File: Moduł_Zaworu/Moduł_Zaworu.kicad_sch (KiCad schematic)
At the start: 10 parts, among them J2 RJ45, J3 RJ45, J9 Screw_Terminal_01x02, Q1 Q_NMOS, U11 ESP32-DEVKITC, U2 HHG1D-1

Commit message: Poprawki schematu modułu zaworu, usunięcie przekaźnika, przygotowanie schematu zasilania
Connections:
- net VSS: now reaches U2.1
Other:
- note added: "mosfet zamiast całego układu bo wystarczy jednostronna konwersja poziomów logicznych"
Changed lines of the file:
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@@
 	(generator_version "9.0")
 	(paper "A4")
+	(text "mosfet zamiast całego układu \nbo wystarczy jednostronna\n konwersja poziomów logicznych"
+		(exclude_from_sim no)
+		(at 129.54 44.45 0)
+		(effects
+			(font
+				(size 1.27 1.27)
+			)
+		)
+	)
 	(text "link RJ45"
 		(exclude_from_sim no)
@@
 	(wire
 		(pts
-			(xy 170.18 41.91) (xy 170.18 71.12)
+			(xy 170.18 40.64) (xy 170.18 71.12)
 		)
 		(stroke
@@
 					(unit 1)
 				)
+			)
+		)
+	)
+	(symbol
+		(lib_id "power:VSS")
+		(at 170.18 40.64 0)
+		(unit 1)
+		(exclude_from_sim no)
+		(in_bom yes)
+		(on_board yes)
+		(dnp no)
+		(fields_autoplaced yes)
+		(property "Reference" "#PWR018"
+			(at 170.18 44.45 0)
+			(effects
+				(font
+					(size 1.27 1.27)
+				)
+				(hide yes)
+			)
+		)
+		(property "Value" "VSS"
+			(at 170.18 35.56 0)
+			(effects
+				(font
+					(size 1.27 1.27)
+				)
+			)
+		)
+		(property "Footprint" ""
+			(at 170.18 40.64 0)
+			(effects
+				(font
+					(size 1.27 1.27)
+				)
+				(hide yes)
+			)
+		)
+		(property "Datasheet" ""
+			(at 170.18 40.64 0)
+			(effects
+				(font
+					(size 1.27 1.27)
+				)
+				(hide yes)
+			)
+		)
+		(property "Description" "Power symbol creates a global label with name \"VSS\""
+			(at 170.18 40.64 0)
+			(effects
+				(font
+					(size 1.27 1.27)
+				)
+				(hide yes)
+			)
+		)
+		(pin "1"
+		)
+		(instances
+			(project "Moduł_Zaworu"
+				(path "/8513fd68-b07b-4062-94bb-7b0327ec704f"
+					(reference "#PWR018")
+					(unit 1)
+				)

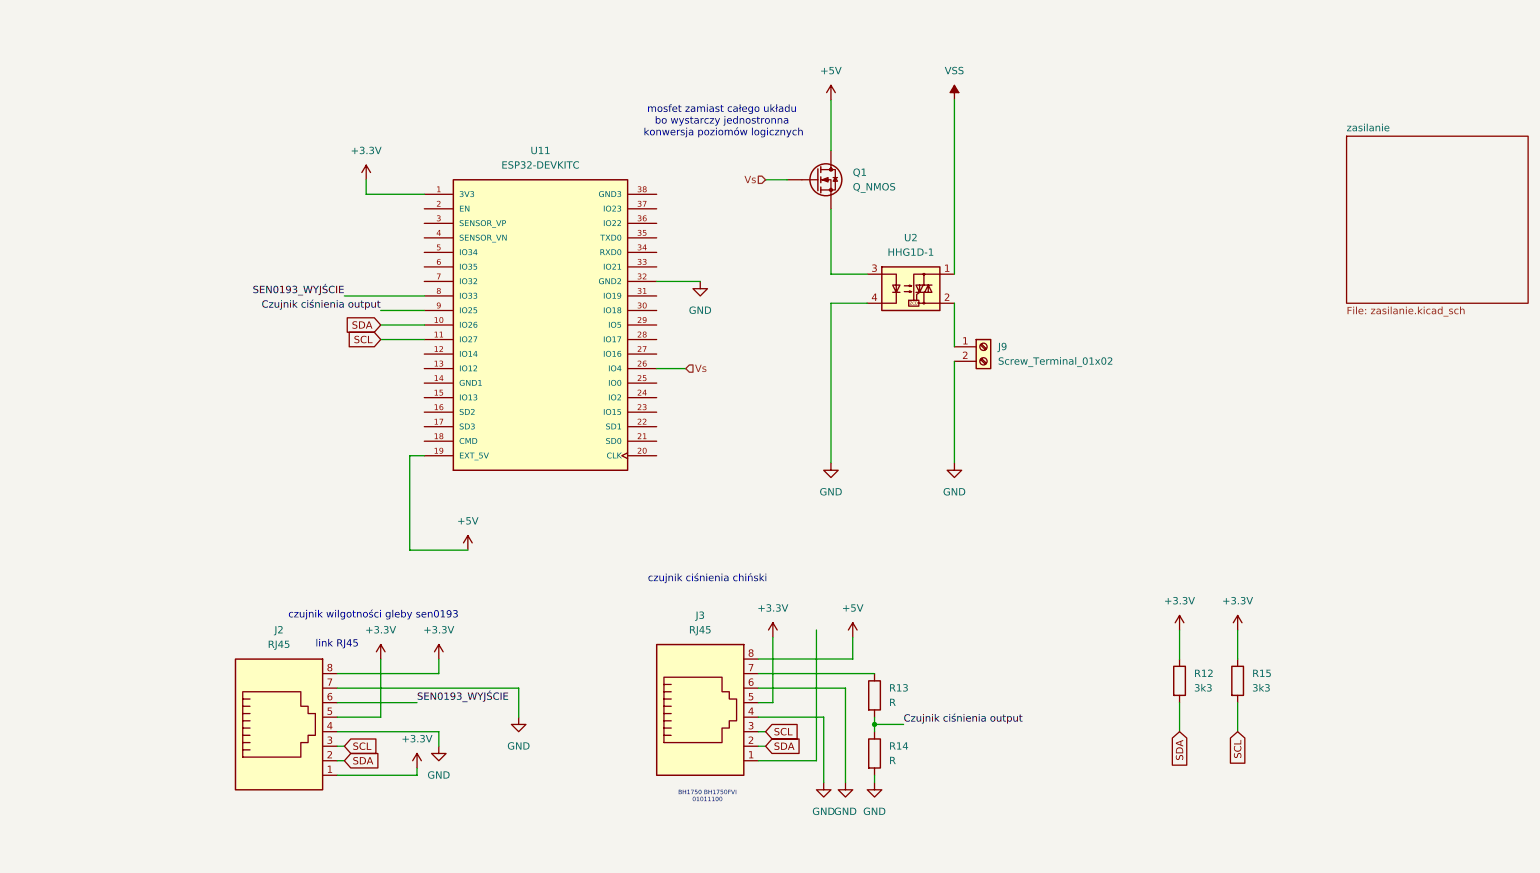
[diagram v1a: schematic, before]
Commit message: Poprawki schematu modułu zaworu, usunięcie przekaźnika, przygotowanie schematu zasilania
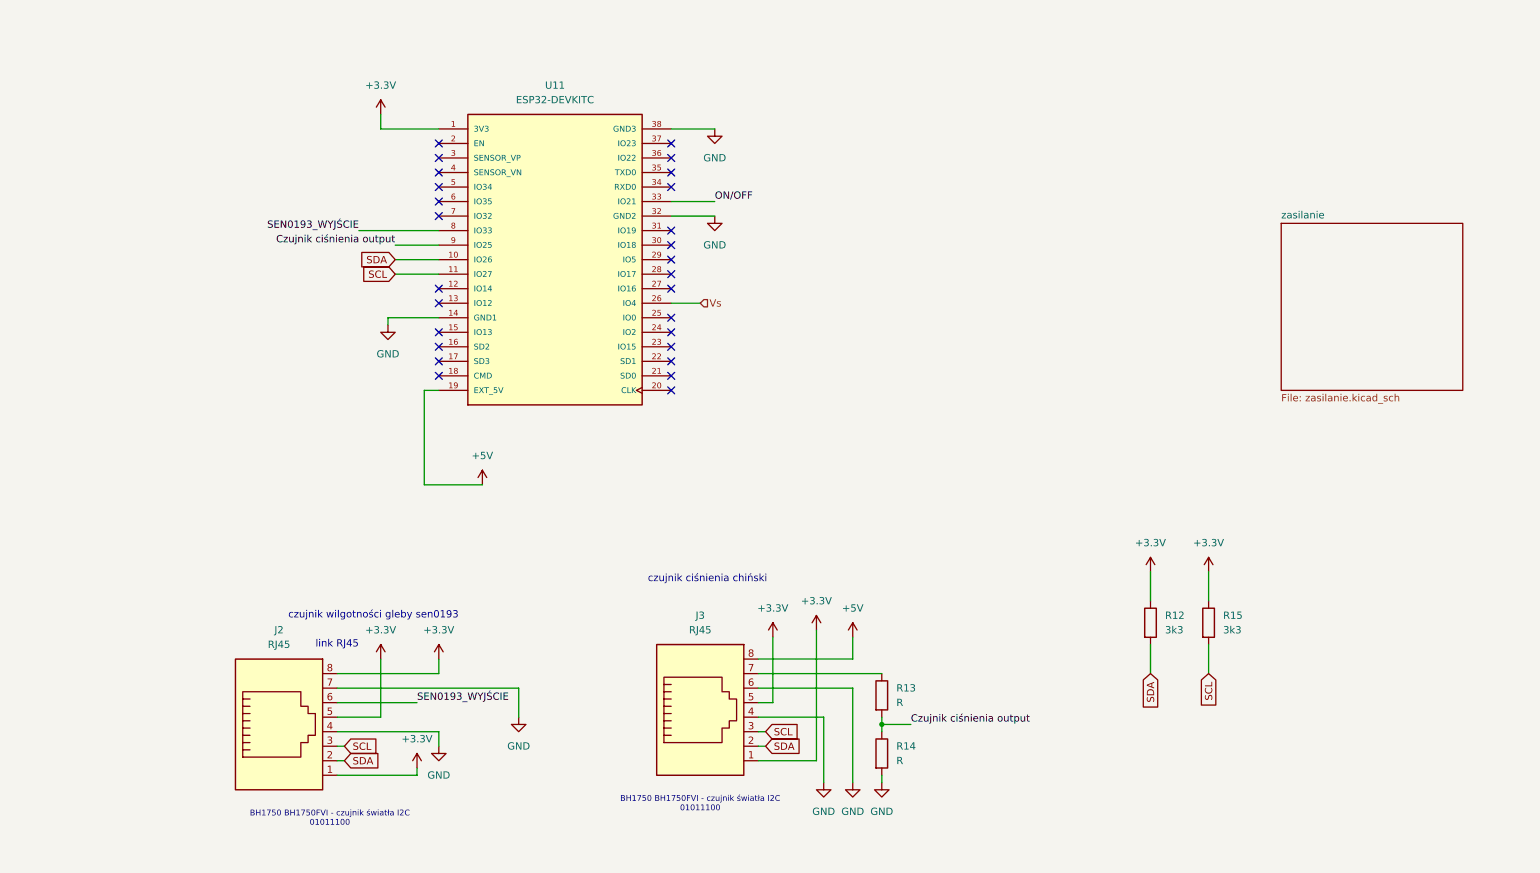
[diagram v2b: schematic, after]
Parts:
- removed J9: Screw_Terminal_01x02, TerminalBlock:TerminalBlock_MaiXu_MX126-5.0-02P_1x02_P5.00mm, symbol Connector:Screw_Terminal_01x02
- removed Q1: Q_NMOS, symbol Device:Q_NMOS
- removed U2: HHG1D-1, Relay_THT:RELAY_G3MB-202P, symbol Relay_SolidState:HHG1D-1
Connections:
- net +3.3V: now also J3.1
- net GND: now also U11.14 (GND1), U11.38 (GND3)
- net ON/OFF: now reaches U11.33 (IO21)
- no-connect marks 0 -> 27
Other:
- note added: "BH1750 BH1750FVI - czujnik światła I2C 01011100"
- note removed: "BH1750 BH1750FVI 01011100"
- note removed: "mosfet zamiast całego układu bo wystarczy jednostronna konwersja poziomów logicznych"
- moved on the sheet: R12, R13, R14, R15, U11

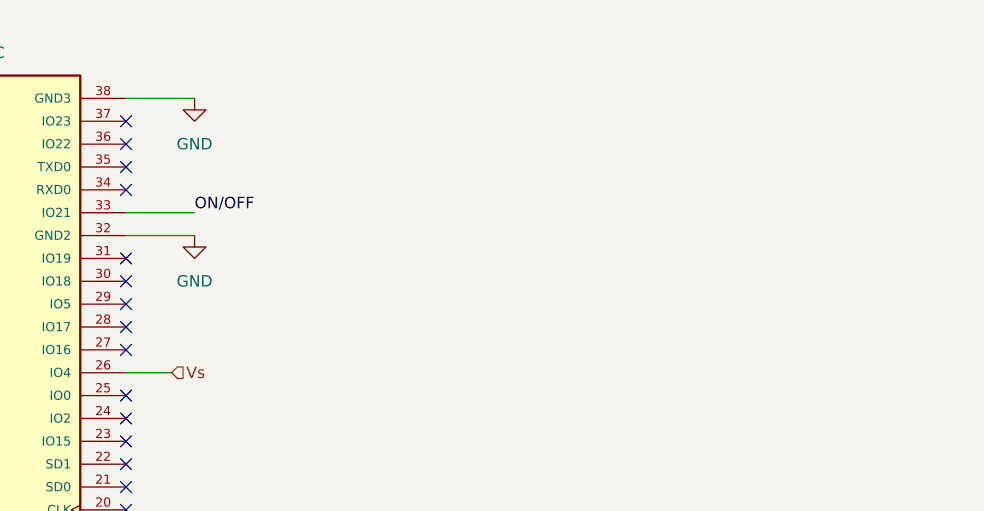
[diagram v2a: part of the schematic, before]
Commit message: Usunięcie zewnętrzego zasilania 12 i stabilizatora napięcia, korekcja zasilania wzmacniacz operacyjny moduł zasilania
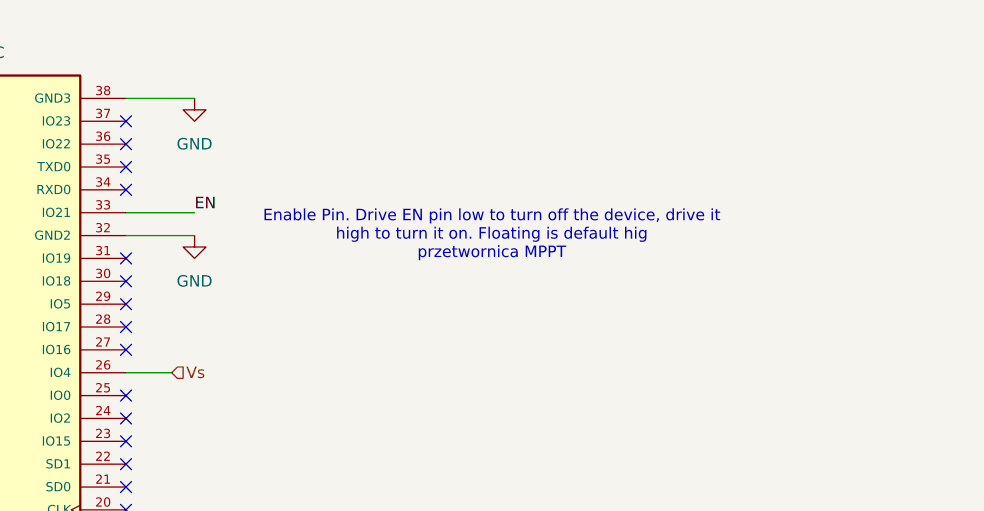
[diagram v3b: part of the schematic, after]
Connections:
- net ON/OFF renamed EN
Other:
- note added: "Enable Pin. Drive EN pin low to turn off the device, drive it high to turn it on. Floating is default hig przetwornica MPPT"
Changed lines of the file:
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@@
+		)
+	)
+	(text "Enable Pin. Drive EN pin low to turn off the device, drive it\nhigh to turn it on. Floating is default hig\nprzetwornica MPPT\n"
+		(exclude_from_sim no)
+		(at 161.29 60.96 0)
+		(effects
+			(font
+				(size 1.27 1.27)
+			)
 		)
 	)
@@
 		)
 	)
-	(label "ON{slash}OFF"
+	(label "EN"
 		(at 128.27 58.42 0)
 		(effects

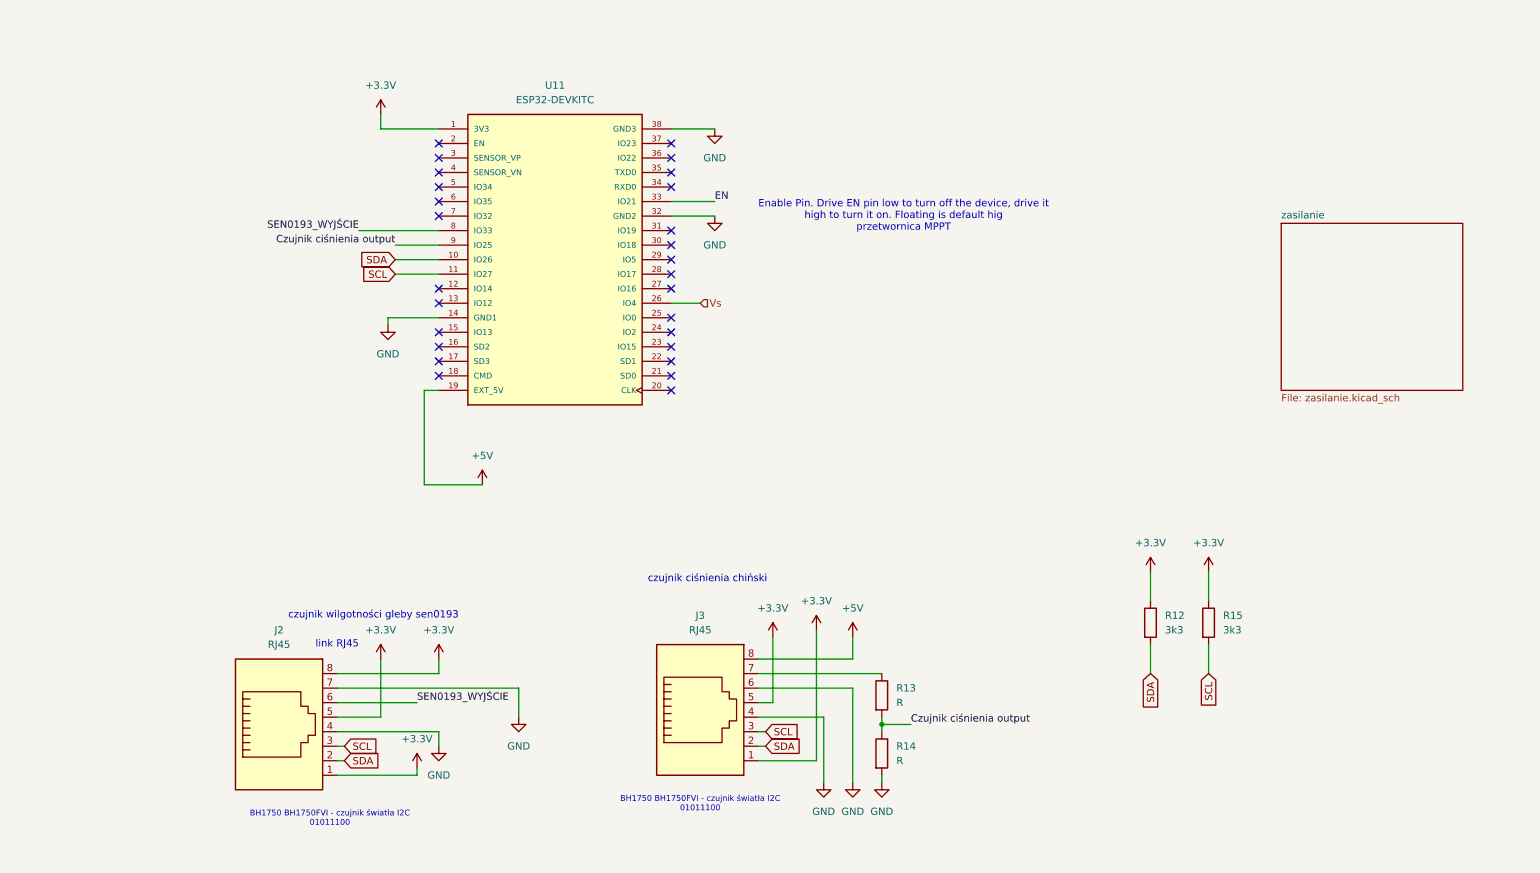
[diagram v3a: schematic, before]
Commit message: Poprawki moduł zasilania, stowrzenie płytki, zostało trochę błędów, zapomniałem dać mouting holes
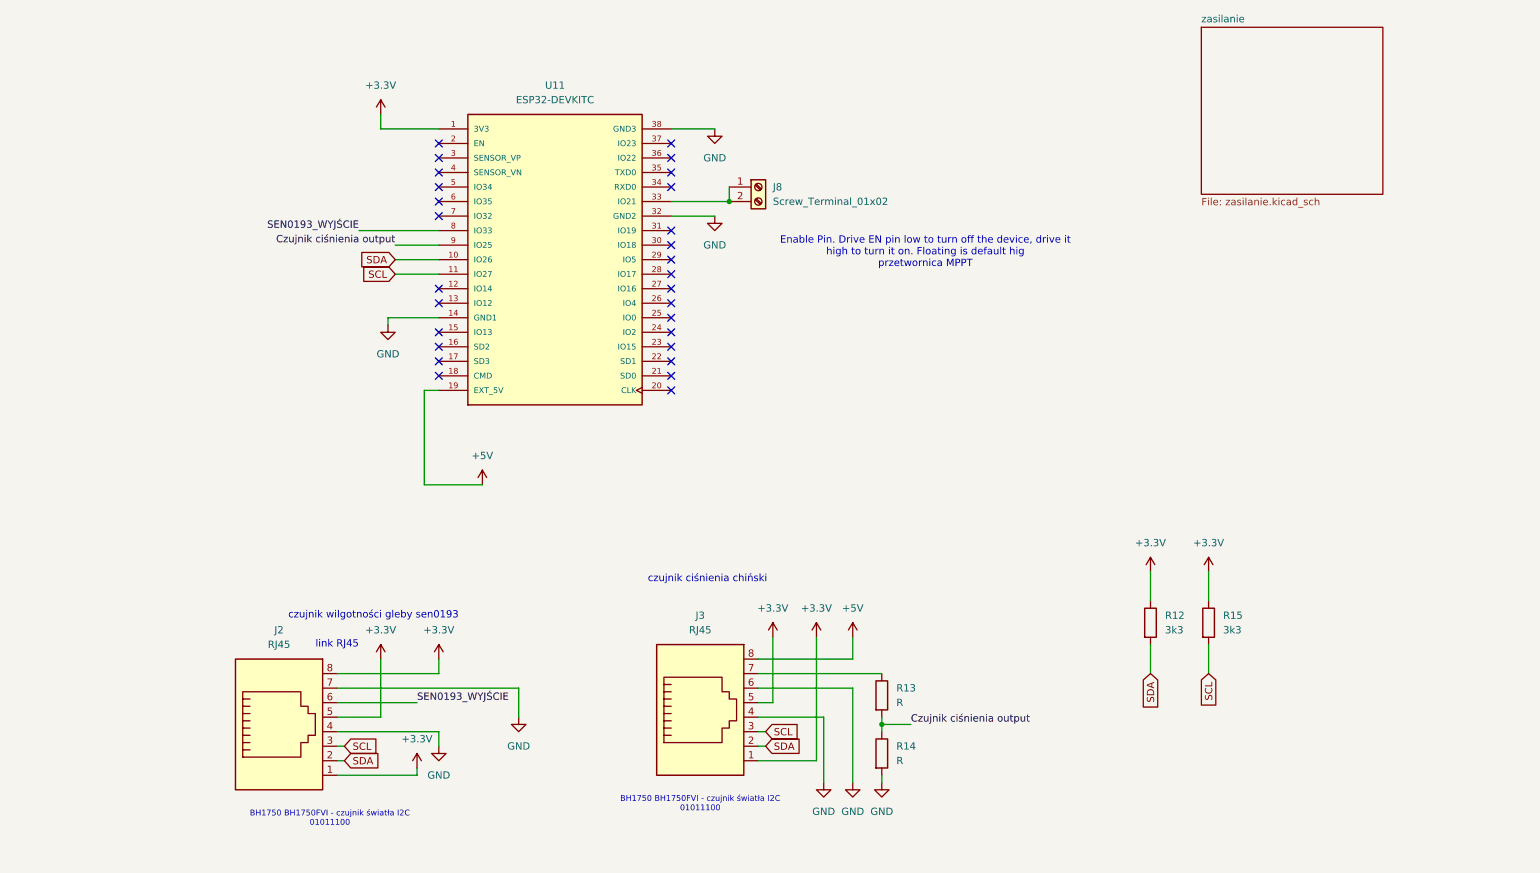
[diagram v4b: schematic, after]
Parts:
- added J8: Screw_Terminal_01x02, TerminalBlock:TerminalBlock_Xinya_XY308-2.54-2P_1x02_P2.54mm_Horizontal, symbol Connector:Screw_Terminal_01x02
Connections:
- net EN: no longer names the net of U11.33 (IO21)
- net EN: now also J8.1 (Pin_1), J8.2 (Pin_2)
- net Vs: no longer names the net of U11.26 (IO4)
- no-connect marks 27 -> 28
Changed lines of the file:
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@@
 	(text "Enable Pin. Drive EN pin low to turn off the device, drive it\nhigh to turn it on. Floating is default hig\nprzetwornica MPPT\n"
 		(exclude_from_sim no)
-		(at 161.29 60.96 0)
+		(at 165.1 67.31 0)
 		(effects
 			(font
@@
 		(color 0 0 0 0)
 	)
+	(junction
+		(at 130.81 58.42)
+		(diameter 0)
+		(color 0 0 0 0)
+	)
 	(no_connect
 		(at 120.65 68.58)
@@
 	)
 	(no_connect
+		(at 120.65 76.2)
+	)
+	(no_connect
 		(at 80.01 58.42)
 	)
@@
 	(wire
 		(pts
-			(xy 120.65 58.42) (xy 128.27 58.42)
+			(xy 120.65 58.42) (xy 130.81 58.42)
 		)
 		(stroke
@@
 	(wire
 		(pts
-			(xy 146.05 156.21) (xy 146.05 133.35)
+			(xy 146.05 156.21) (xy 146.05 134.62)
 		)
 		(stroke
@@
 	(wire
 		(pts
+			(xy 130.81 55.88) (xy 130.81 58.42)
+		)
+		(stroke
+			(width 0)
+			(type default)
+		)
+	)
+	(wire
+		(pts
 			(xy 62.23 143.51) (xy 93.98 143.51)
 		)
@@
 		(pts
 			(xy 157.48 149.86) (xy 157.48 151.13)
-		)
-		(stroke
-			(width 0)
-			(type default)
-		)
-	)
-	(wire
-		(pts
-			(xy 120.65 76.2) (xy 125.73 76.2)
 		)
 		(stroke
@@
 		)
 	)
-	(label "EN"
-		(at 128.27 58.42 0)
-		(effects
-			(font
-				(size 1.27 1.27)
-			)
-			(justify left bottom)
-		)
-	)
 	(label "Czujnik ciśnienia output"
 		(at 72.39 66.04 180)
@@
 		)
 	)
-	(hierarchical_label "Vs"
-		(shape input)
-		(at 125.73 76.2 0)
-		(effects
-			(font
-				(size 1.27 1.27)
-			)
-			(justify left)
-		)
-	)
 	(symbol
 		(lib_id "power:+3.3V")
@@
 	)
 	(symbol
+		(lib_id "Connector:Screw_Terminal_01x02")
+		(at 135.89 55.88 0)
+		(unit 1)
+		(exclude_from_sim no)
+		(in_bom yes)
+		(on_board yes)
+		(dnp no)
+		(fields_autoplaced yes)
+		(property "Reference" "J8"
+			(at 138.43 55.8799 0)
+			(effects
+				(font
+					(size 1.27 1.27)
+				)
+				(justify left)
+			)
+		)
+		(property "Value" "Screw_Terminal_01x02"
+			(at 138.43 58.4199 0)
+			(effects
+				(font
+					(size 1.27 1.27)
+				)
+				(justify left)
+			)
+		)
+		(property "Footprint" "TerminalBlock:TerminalBlock_Xinya_XY308-2.54-2P_1x02_P2.54mm_Horizontal"
+			(at 135.89 55.88 0)
+			(effects
+				(font
+					(size 1.27 1.27)
+				)
+				(hide yes)
+			)
+		)
+		(property "Datasheet" "~"
+			(at 135.89 55.88 0)
+			(effects
+				(font
+					(size 1.27 1.27)
+				)
+				(hide yes)
+			)
+		)
+		(property "Description" "Generic screw terminal, single row, 01x02, script generated (kicad-library-utils/schlib/autogen/connector/)"
+			(at 135.89 55.88 0)
+			(effects
+				(font
+					(size 1.27 1.27)
+				)
+				(hide yes)
+			)
+		)
+		(pin "1"
+		)
+		(pin "2"
+		)
+		(instances
+			(project ""
+				(path "/8513fd68-b07b-4062-94bb-7b0327ec704f"
+					(reference "J8")
+					(unit 1)
+				)
+			)
+		)
+	)
+	(symbol
 		(lib_id "power:GND")
 		(at 157.48 160.02 0)
@@
 	(symbol
 		(lib_id "power:+3.3V")
-		(at 146.05 133.35 0)
+		(at 146.05 134.62 0)
 		(unit 1)
 		(exclude_from_sim no)
@@
 		(fields_autoplaced yes)
 		(property "Reference" "#PWR08"
-			(at 146.05 137.16 0)
+			(at 146.05 138.43 0)
 			(effects
 				(font
@@
 		)
 		(property "Value" "+3.3V"
-			(at 146.05 128.27 0)
+			(at 146.05 129.54 0)
 			(effects
 				(font
@@
 		)
 		(property "Footprint" ""
-			(at 146.05 133.35 0)
+			(at 146.05 134.62 0)
 			(effects
 				(font
@@
 		)
 		(property "Datasheet" ""
-			(at 146.05 133.35 0)
+			(at 146.05 134.62 0)
 			(effects
 				(font
@@
 		)
 		(property "Description" "Power symbol creates a global label with name \"+3.3V\""
-			(at 146.05 133.35 0)
+			(at 146.05 134.62 0)
 			(effects
 				(font
@@
 	)
 	(sheet
-		(at 227.33 62.23)
+		(at 213.36 27.94)
 		(size 31.75 29.21)
 		(exclude_from_sim no)
@@
 		)
 		(property "Sheetname" "zasilanie"
-			(at 227.33 61.5184 0)
+			(at 213.36 27.2284 0)
 			(effects
 				(font
@@
 		)
 		(property "Sheetfile" "zasilanie.kicad_sch"
-			(at 227.33 92.0246 0)
-			(effects
-				(font
+			(at 213.36 57.7346 0)
+			(effects
+				(font
